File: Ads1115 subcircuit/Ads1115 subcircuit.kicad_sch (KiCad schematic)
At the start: 5 parts, among them J1 Conn_01x03_Socket, J2 Conn_01x03_Socket, J3 Conn_01x03_Socket, J4 Conn_01x03_Socket, U1 ADS1115IDGS

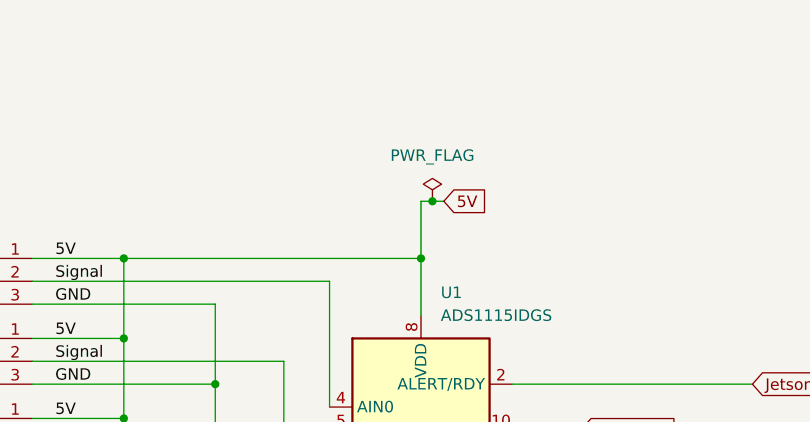
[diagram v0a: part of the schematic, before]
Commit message: Version 2 of ADS1115 Subcircuit
Change power voltage to 3.3V and added 100 nF decoupling capacitor
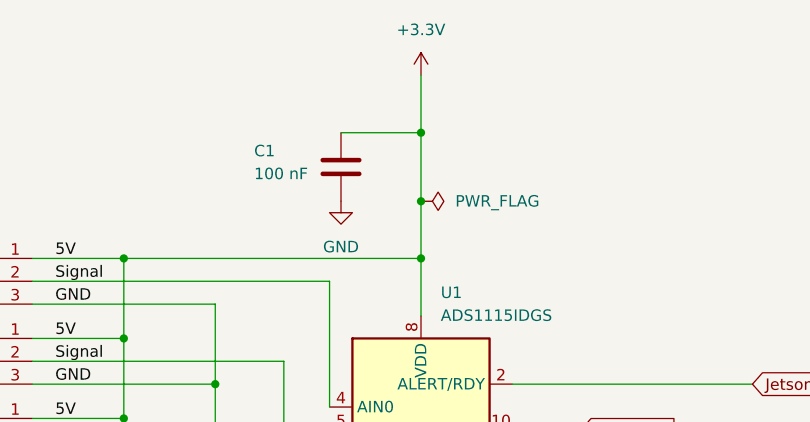
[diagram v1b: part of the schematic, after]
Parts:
- added C1: 100 nF, symbol Device:C
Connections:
- net GND: now also C1.2
- net 5V renamed +3.3V
- net +3.3V: now also C1.1

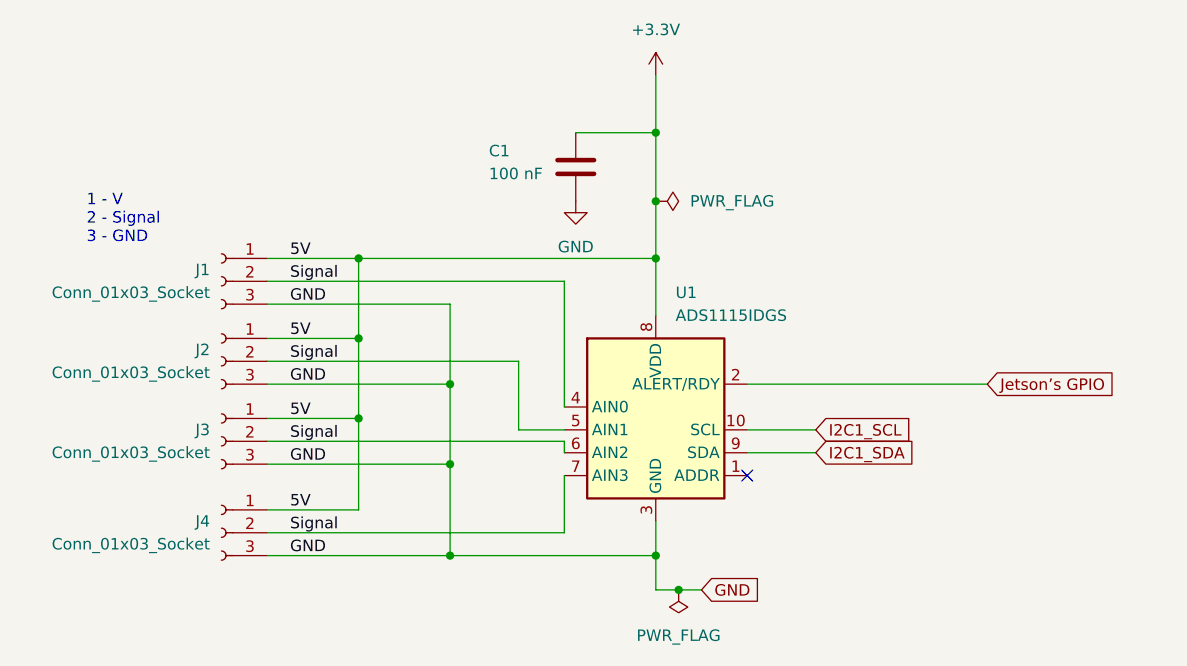
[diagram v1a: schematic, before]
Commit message: ADS1115 Subcircuit V3
Added footprint for the capacitor & changed voltage values on terminal inputs to 3.3V
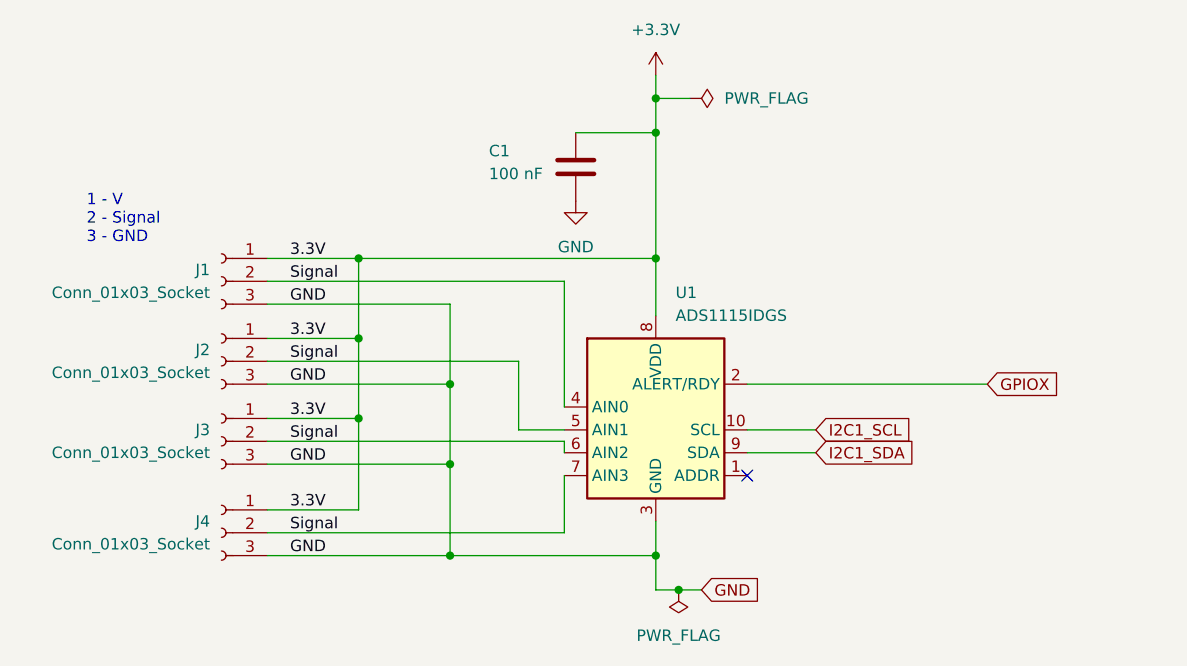
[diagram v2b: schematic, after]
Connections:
- net Jetson’s GPIO renamed GPIOX
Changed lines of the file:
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@@
 	)
 	(junction
-		(at 123.19 68.58)
+		(at 123.19 57.15)
 		(diameter 0)
 		(color 0 0 0 0)
@@
 	(wire
 		(pts
-			(xy 123.19 54.61) (xy 123.19 60.96)
+			(xy 123.19 54.61) (xy 123.19 57.15)
+		)
+		(stroke
+			(width 0)
+			(type default)
+			(color 255 0 0 1)
+		)
+	)
+	(wire
+		(pts
+			(xy 123.19 57.15) (xy 123.19 60.96)
 		)
 		(stroke
@@
 	(wire
 		(pts
-			(xy 123.19 60.96) (xy 123.19 68.58)
+			(xy 123.19 60.96) (xy 123.19 74.93)
 		)
 		(stroke
@@
 	(wire
 		(pts
-			(xy 123.19 68.58) (xy 123.19 74.93)
-		)
-		(stroke
-			(width 0)
-			(type default)
-			(color 255 0 0 1)
-		)
-	)
-	(wire
-		(pts
 			(xy 133.35 93.98) (xy 140.97 93.98)
 		)
@@
 		(pts
 			(xy 114.3 60.96) (xy 123.19 60.96)
+		)
+		(stroke
+			(width 0)
+			(type default)
+		)
+	)
+	(wire
+		(pts
+			(xy 123.19 57.15) (xy 127 57.15)
 		)
 		(stroke
@@
 		)
 	)
-	(label "5V"
+	(label "3.3V"
 		(at 82.55 92.71 0)
 		(fields_autoplaced yes)
@@
 		)
 	)
-	(label "5V"
+	(label "3.3V"
 		(at 82.55 83.82 0)
 		(fields_autoplaced yes)
@@
 		)
 	)
-	(label "5V"
+	(label "3.3V"
 		(at 82.55 102.87 0)
 		(fields_autoplaced yes)
@@
 		)
 	)
-	(label "5V"
+	(label "3.3V"
 		(at 82.55 74.93 0)
 		(fields_autoplaced yes)
@@
 		)
 	)
-	(global_label "Jetson’s GPIO"
+	(global_label "GPIOX"
 		(shape input)
 		(at 160.02 88.9 0)
@@
 		)
 		(property "Intersheetrefs" "${INTERSHEET_REFS}"
-			(at 176.189 88.9 0)
+			(at 168.69 88.9 0)
 			(effects
 				(font
@@
 	(symbol
 		(lib_id "power:PWR_FLAG")
-		(at 123.19 68.58 270)
+		(at 127 57.15 270)
 		(unit 1)
 		(exclude_from_sim no)
@@
 		(fields_autoplaced yes)
 		(property "Reference" "#FLG01"
-			(at 125.095 68.58 0)
+			(at 128.905 57.15 0)
 			(effects
 				(font
@@
 		)
 		(property "Value" "PWR_FLAG"
-			(at 127 68.5799 90)
+			(at 130.81 57.1499 90)
 			(effects
 				(font
@@
 		)
 		(property "Footprint" ""
-			(at 123.19 68.58 0)
+			(at 127 57.15 0)
 			(effects
 				(font
@@
 		)
 		(property "Datasheet" "~"
-			(at 123.19 68.58 0)
+			(at 127 57.15 0)
 			(effects
 				(font
@@
 		)
 		(property "Description" "Special symbol for telling ERC where power comes from"
-			(at 123.19 68.58 0)
-			(effects
-				(font
+			(at 127 57.15 0)
+			(effects
+				(font
